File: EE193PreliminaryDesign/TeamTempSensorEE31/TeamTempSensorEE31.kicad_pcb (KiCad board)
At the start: 2 copper layers, 27.4 x 33.7 mm, 39 parts, among them J1 USB_B_Micro, J2 Battery_Connector, Q1 BS170F, Q2 BC818, Q3 BC818, Q4 NTA4151PT1G, SW1 SW_DIP_x01, U1 CP2102N-A02-GQFN28, U2 MCP9808_MSOP, U3 LD1117S33TR_SOT223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

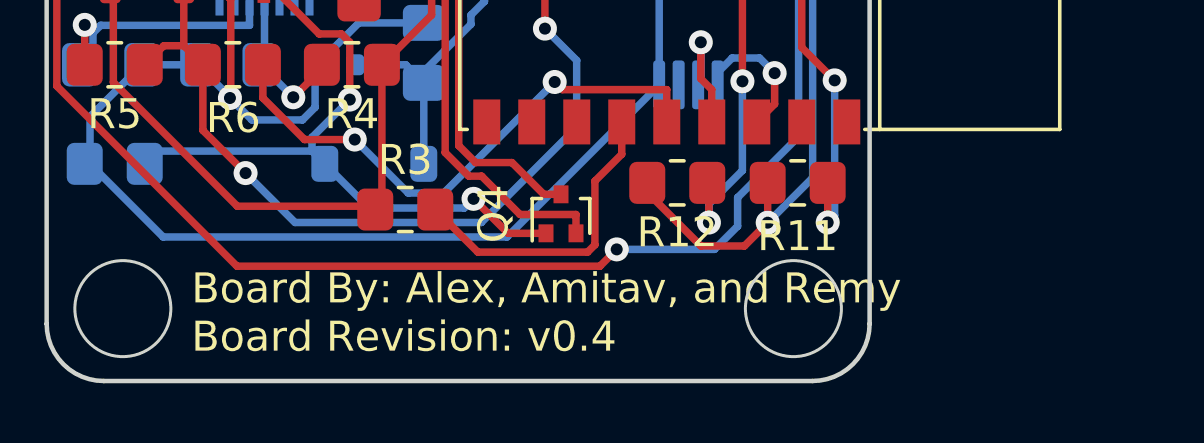
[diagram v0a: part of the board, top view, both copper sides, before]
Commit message: change font on v0.4
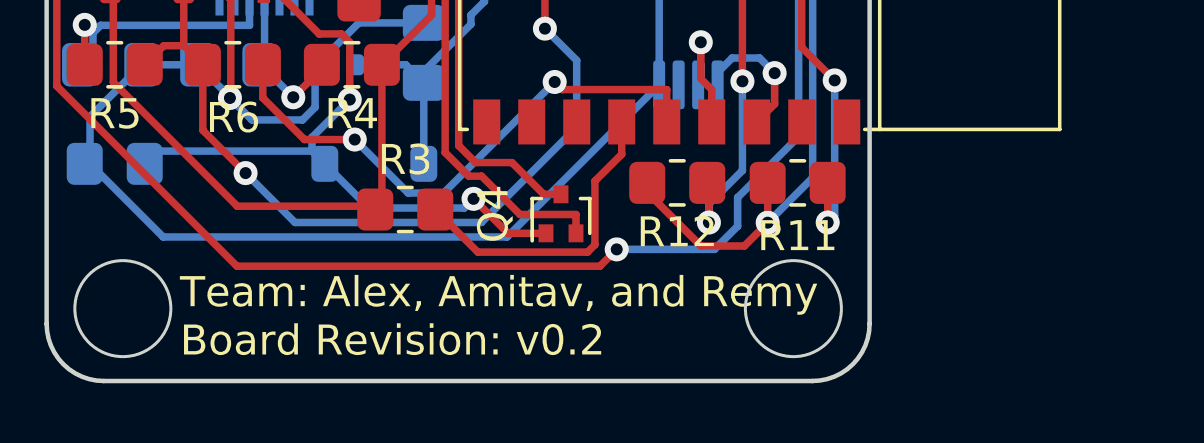
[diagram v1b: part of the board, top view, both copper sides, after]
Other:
- board text added: "Team: Alex, Amitav, and Remy Board Revision: v0.2"
- board text added: "Tufts EE193 Net. Embed. Sys. Prof. Bell - Don't Move Me!"
- board text removed: "Board By: Alex, Amitav, and Remy Board Revision: v0.4"
- board text removed: "Tufts EE193: Net. Embedded Sys. Prof. Bell - Don't Move Me!"
